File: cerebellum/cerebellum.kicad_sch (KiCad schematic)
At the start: 184 parts, among them J1 PWR_OUT, J2 PWR_IN, J5 CM4_A, J6 CM4_B, J7 RJ45, Q1 AP2300, U1 GD32F405VGHx, U2 TPS5430DDAR, U3 BMI088, U4 TCAN4550RGYRQ1, U5 ICP-20100, U6 TPS54231, U7 TCAN4550RGYRQ1, Y1 8M, Y2 40M, Y3 40M

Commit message: [New] Complete cerebellum
* Refactor cerebellum, now cerebellum includes features of heart &
  cerebellum

Signed-off-by: Homalozoa <nx.tardis@gmail.com>
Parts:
- removed C33, C34: 8.2pF, 10%, 50V, Capacitor_SMD:C_0402_1005Metric, symbol Device:C
- removed C35: 10nF, 10%, 50V, Capacitor_SMD:C_0402_1005Metric, symbol Device:C
- removed C36: 470nF, 10%, 50V, Capacitor_SMD:C_0603_1608Metric, symbol Device:C
- removed C37, C38: 100pF, 10%, 10V, Capacitor_SMD:C_0402_1005Metric, symbol Device:C
- removed C39: 100nF, 10%, 50V, Capacitor_SMD:C_0402_1005Metric, symbol Device:C
- removed C40, C41: 10uF, 10%, 50V, Capacitor_SMD:C_0603_1608Metric, symbol Device:C
- removed C42, C43: 4.7uF 50V, Capacitor_SMD:C_0805_2012Metric, symbol Device:C
- removed C44: 10uf 50V, Capacitor_SMD:C_0402_1005Metric, symbol Device:C
- removed C45: 1.5nf 50V, Capacitor_SMD:C_0603_1608Metric, symbol Device:C
- removed C46: 8.2nf 50V, Capacitor_SMD:C_0603_1608Metric, symbol Device:C
- removed C47: 10pf 50V, Capacitor_SMD:C_0402_1005Metric, symbol Device:C
- removed C48, C? (x11): 100nF, 10%, 10V, Capacitor_SMD:C_0402_1005Metric, symbol Device:C
- removed C49, C50, C? (x12): 47uf 50V, Capacitor_SMD:C_0603_1608Metric, symbol Device:C
- removed C? (x2): 22pF, 10%, 50V, Capacitor_SMD:C_0402_1005Metric, symbol Device:C
- removed C? (x10): 100nF, 10%, 10V, Capacitor_SMD:C_0201_0603Metric, symbol Device:C
- removed C? (x3): 1uF, 10%, 10V, Capacitor_SMD:C_0402_1005Metric, symbol Device:C
- removed C?: 3nF, 10V, Capacitor_SMD:C_0402_1005Metric, symbol Device:C
- removed C? (x2): 10uF, 10%, 10V, Capacitor_SMD:C_0402_1005Metric, symbol Device:C
- removed C?: 4.7uF, 10%, 10V, Capacitor_SMD:C_0402_1005Metric, symbol Device:C
- removed D5: B240, Diode_SMD:D_SMB, symbol Diode:B240
- removed J1: PWR_OUT, Rolling_Custom:XT30PW(2+2), symbol Rolling_Custom:XT30PW(2+2)
- removed J2: PWR_IN, Rolling_Custom:XT30PW(2+2), symbol Rolling_Custom:XT30PW(2+2)
- removed J5: CM4_A, Rolling_Custom:HRS_DF40C-100DS-0.4V(51), symbol Rolling_Custom:DF40C-100DS-0.4V(51)
- removed J6: CM4_B, Rolling_Custom:HRS_DF40C-100DS-0.4V(51), symbol Rolling_Custom:DF40C-100DS-0.4V(51)
- removed J7: RJ45, Connector_RJ:RJ45_Molex_0855135013_Vertical, symbol Connector:RJ45
- removed J? (x4): USB_C_Receptacle, Rolling_Custom:USB_C_Receptacle_TYPE-C-324G-BCP24, symbol Connector:USB_C_Receptacle
- removed J?: (no value), symbol Connector:USB_C_Receptacle_USB2.0
- removed L3: 15uh, Inductor_SMD:L_0603_1608Metric, symbol Device:L
- removed L?: 0R, Resistor_SMD:R_0402_1005Metric, symbol Device:L_Ferrite
- removed R16: 3k, Resistor_SMD:R_0402_1005Metric, symbol Device:R_US
- removed R17: 169k, Resistor_SMD:R_0402_1005Metric, symbol Device:R_US
- removed R18: 20.5, Resistor_SMD:R_0402_1005Metric, symbol Device:R_US
- removed R19: 64.9k, Resistor_SMD:R_0402_1005Metric, symbol Device:R_US
- removed R20: 10.2k, Resistor_SMD:R_0402_1005Metric, symbol Device:R_US
- removed R21: 1.96k, Resistor_SMD:R_0402_1005Metric, symbol Device:R_US
- removed R? (x3): 4.7k, Resistor_SMD:R_0402_1005Metric, symbol Device:R_US
- removed R? (x2): 47k, Resistor_SMD:R_0402_1005Metric, symbol Device:R_US
- removed R?: 2.2k, Resistor_SMD:R_0201_0603Metric, symbol Device:R_US
- removed R?: (no value), Resistor_SMD:R_0201_0603Metric, symbol Device:R_US
- removed R? (x4): 100k, Resistor_SMD:R_0402_1005Metric, symbol Device:R_US
- removed R?: 15k, Resistor_SMD:R_0402_1005Metric, symbol Device:R_US
- removed R?: 1M, Resistor_SMD:R_0402_1005Metric, symbol Device:R_US
- removed U6: TPS54231, Package_SO:SOIC-8_3.9x4.9mm_P1.27mm, symbol Regulator_Switching:TPS54233
- removed U7: TCAN4550RGYRQ1, Rolling_Custom:VQFN20, symbol Rolling_Custom:TCAN4550RGYRQ1
- removed U? (x4): APL3553, Package_TO_SOT_SMD:SOT-23-5, symbol Rolling_Custom:APL3553
- removed U? (x7): TPD4EUSB30, Package_SON:USON-10_2.5x1.0mm_P0.5mm, symbol Power_Protection:TPD4EUSB30
- removed U? (x4): ECMF04-4HSM10, Rolling_Custom:SON_4-4HSM10_STM, symbol Rolling_Custom:ECMF04-4HSM10
- removed U?: AP2127K-ADJ, Package_TO_SOT_SMD:SOT-23-5, symbol Regulator_Linear:AP2127K-ADJ
- removed U? (x4): ECMF02-4CMX8, Rolling_Custom:MICRO_QFN-8L_STM, symbol Rolling_Custom:ECMF02-4CMX8
- removed U?: UPD720201K8-701-BAC-A, Rolling_Custom:QFN40P800X800X90-69N, symbol Rolling_Custom:UPD720201K8-701-BAC-A
- removed U?: GD25Q40C, symbol Rolling_Custom:GD25Q40C
- removed U?: (no value), symbol Power_Protection:TPD4EUSB30
- removed Y3: 40M, Oscillator:Oscillator_SMD_EuroQuartz_XO32-4Pin_3.2x2.5mm, symbol Device:Crystal_GND24
- removed Y?: 24M, Oscillator:Oscillator_SMD_EuroQuartz_XO32-4Pin_3.2x2.5mm, symbol Device:Crystal_GND24
- added FB1: 220R, Resistor_SMD:R_0603_1608Metric, symbol Device:FerriteBead
- added J1: Power_IN, Rolling_Custom:AMASS_XT60PW-F, symbol Rolling_Custom:XT60PW-F
- added J10: Arm_R, Rolling_Custom:XT30PW(2+2), symbol Rolling_Custom:XT30PW(2+2)
- added J11: Light, Rolling_Custom:XT30PW(2+2), symbol Rolling_Custom:XT30PW(2+2)
- added J2: Power_Back, Rolling_Custom:AMASS_XT60PW-M, symbol Rolling_Custom:XT60PW-M
- added J5: Head, Rolling_Custom:XT30PW(2+2), symbol Rolling_Custom:XT30PW(2+2)
- added J7: Leg_L, Rolling_Custom:XT30PW(2+2), symbol Rolling_Custom:XT30PW(2+2)
- added J8: Leg_R, Rolling_Custom:XT30PW(2+2), symbol Rolling_Custom:XT30PW(2+2)
- added J9: Arm_L, Rolling_Custom:XT30PW(2+2), symbol Rolling_Custom:XT30PW(2+2)
- added Q2, Q3, Q4: FH1404G6, Rolling_Custom:PDFN5X6-8L, symbol Rolling_Custom:WNM6006
- J3, J4: value (none) -> GD_LINK
- R8: value 33k -> 120R
- U1: value GD32F405VGHx -> (none); footprint Package_BGA:UFBGA-100_7x7mm_Layout12x12_P0.5mm -> Rolling_Custom:Modified-BGA-100_7x7mm_Layout12x12_P0.5mm
- gave numbers to parts that had none: 1
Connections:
- net TCANPi_WAKE is gone; now on net CAN_H: R8.1
- net +24V: now also J1.1 (+), Q2.5
- net ACC_SCS: now also U1.A12 (PA12); no longer U1.A9 (PA15)
- net BMI_HEAT: now also U1.A3 (PB8); no longer U1.H10 (PD15)
- net CAN_H: now also J10.3 (CAN_H), J11.3 (CAN_H), J5.3 (CAN_H), J7.3 (CAN_H), J8.3 (CAN_H), J9.3 (CAN_H)
- net CAN_L: now also R8.2, J10.4 (CAN_L), J11.4 (CAN_L), J5.4 (CAN_L), J7.4 (CAN_L), J8.4 (CAN_L), J9.4 (CAN_L)
- net GND: now also FB1.2; no longer C13.2, D1.1 (A1)
- net GYRO_SCS: now also U1.A9 (PA15); no longer U1.A12 (PA12)
- net PWRCT_3: now reaches U1.A1 (PE3)
- net PWRCT_3: now also Q4.4
- net PWRCT_2: now reaches U1.B1 (PE4)
- net PWRCT_2: now also Q3.4
- net PWRCT_1: now reaches U1.C1 (PC13)
- net PWRCT_1: now also Q2.4
- net BMI_INT1: no longer names the net of U3.16 (INT1)
- net BMI_INT1: no longer U1.E10 (PC8)
- net BMI_INT2: no longer names the net of U3.1 (INT2)
- net BMI_INT2: no longer U1.D10 (PA9)
- net BMI_INT3: no longer names the net of U3.12 (INT3)
- net BMI_INT3: no longer U1.C8 (PD2)
- net BMI_INT4: no longer names the net of U3.13 (INT4)
- net BMI_INT4: no longer U1.B7 (PD4)
- new net EXT_PWR: J2.1 (+), Q3.5, Q4.1, Q4.2, Q4.3
- new net GNDA: C13.2, D1.1 (A1), FB1.1, J1.2 (-), J1.S1 (SHIELD), J1.S2 (SHIELD), J10.2 (GND), J11.2 (GND), J2.2 (-), J2.S1 (SHIELD), J2.S2 (SHIELD), J5.2 (GND), J7.2 (GND), J8.2 (GND), J9.2 (GND)
- new net PWR_EXPORT: J10.1 (VBUS), J11.1 (VBUS), J5.1 (VBUS), J7.1 (VBUS), J8.1 (VBUS), J9.1 (VBUS), Q2.1, Q2.2, Q2.3, Q3.1, Q3.2, Q3.3, Q4.5
- no-connect marks 169 -> 65
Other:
- moved on the sheet: C1, C10, C11, C12, C13, C14, C15, C16, C17, C18, C19, C2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

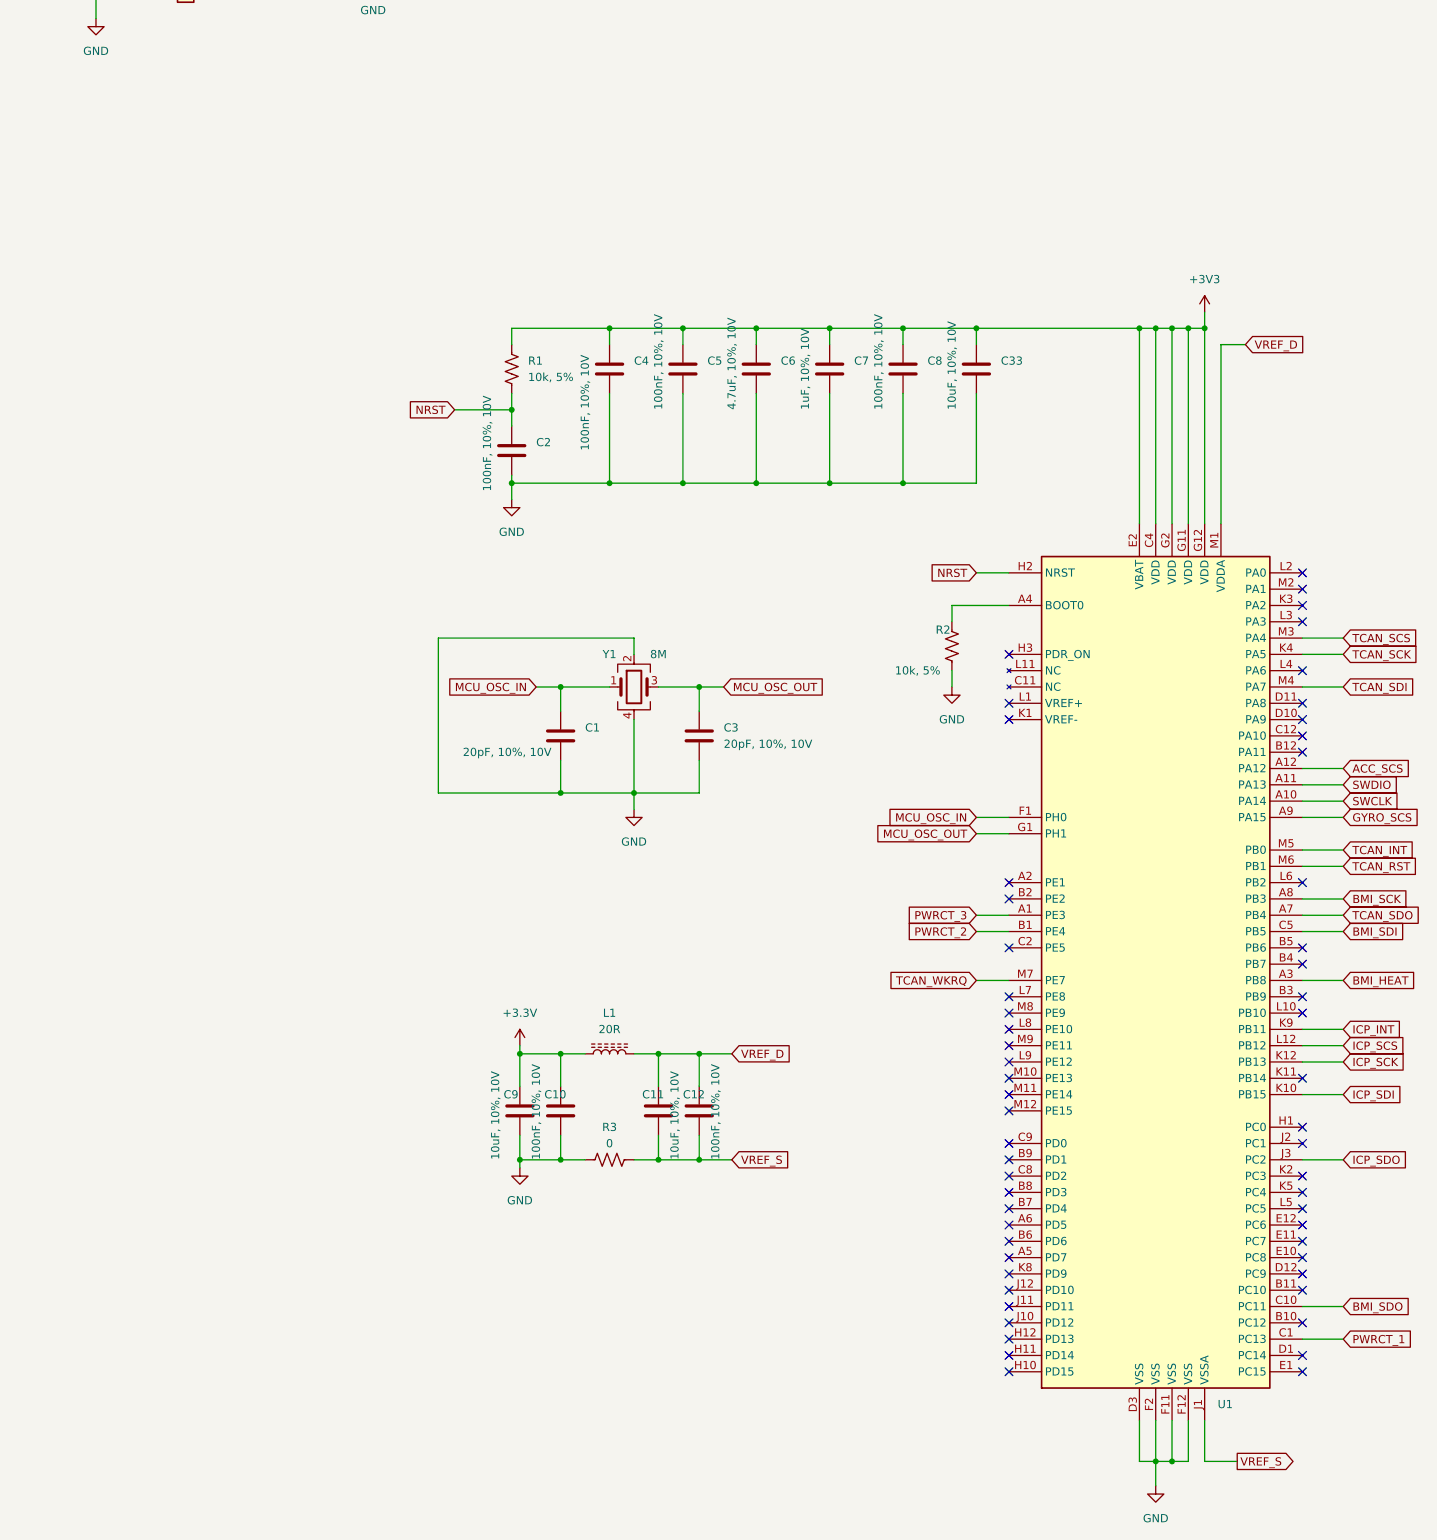
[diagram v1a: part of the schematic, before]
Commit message: [New] Add some capacities to cerebellum
Signed-off-by: Homalozoa <nx.tardis@gmail.com>
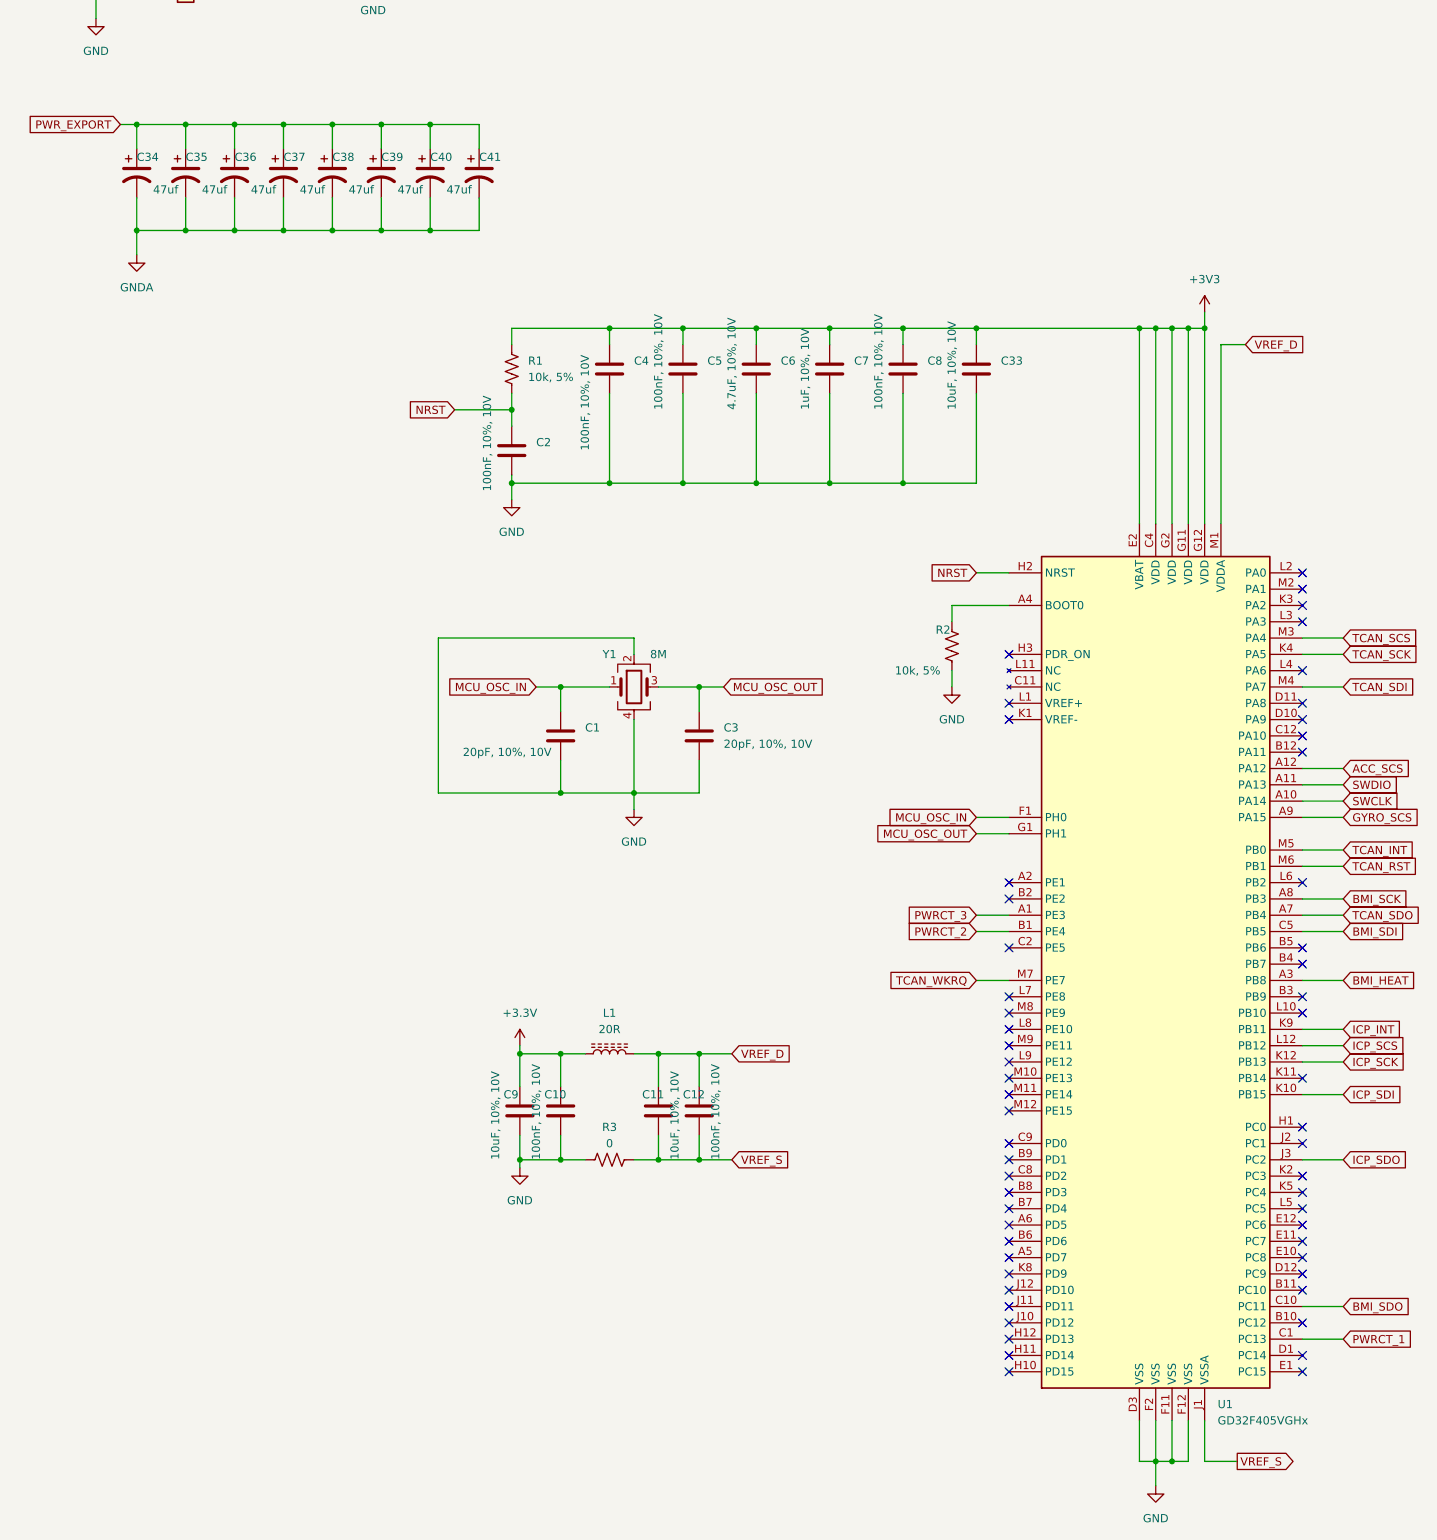
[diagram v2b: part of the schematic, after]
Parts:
- added C34: (no value), symbol Device:C_Polarized_US
- added C35, C36, C37, C38, C39, C40, C41: 47uf, Capacitor_SMD:CP_Elec_8x6.2, symbol Device:C_Polarized_US
- U1: value (none) -> GD32F405VGHx
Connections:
- net GNDA: now also C34.2, C35.2, C36.2, C37.2, C38.2, C39.2, C40.2, C41.2
- net PWR_EXPORT: now also C34.1, C35.1, C36.1, C37.1, C38.1, C39.1, C40.1, C41.1

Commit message: [Fix] Fix package of diode in cerebellum
Signed-off-by: Homalozoa <nx.tardis@gmail.com>
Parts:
- C34: value (none) -> 47uf; footprint (none) -> Capacitor_SMD:CP_Elec_8x6.2
- D1: value 30V -> (none); footprint Diode_SMD:D_SMA -> (none)
- D2: value B340 -> ESD5Z3V3; footprint Diode_SMD:D_SMC -> Diode_SMD:D_SOD-523
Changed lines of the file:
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@@
       (effects (font (size 1.27 1.27)) (justify right))
     )
-    (property "Value" "30V" (id 1) (at 353.06 100.33 90)
-      (effects (font (size 1.27 1.27)) (justify right))
-    )
-    (property "Footprint" "Diode_SMD:D_SMA" (id 2) (at 360.68 99.06 0)
+    (property "Value" "" (id 1) (at 353.06 100.33 90)
+      (effects (font (size 1.27 1.27)) (justify right))
+    )
+    (property "Footprint" "" (id 2) (at 360.68 99.06 0)
       (effects (font (size 1.27 1.27)) hide)
     )
@@
       (effects (font (size 1.27 1.27)) (justify left))
     )
-    (property "Value" "" (id 1) (at 44.45 166.37 0)
-      (effects (font (size 1.27 1.27)) (justify left))
-    )
-    (property "Footprint" "" (id 2) (at 49.53 163.83 0)
+    (property "Value" "47uf" (id 1) (at 44.45 166.37 0)
+      (effects (font (size 1.27 1.27)) (justify left))
+    )
+    (property "Footprint" "Capacitor_SMD:CP_Elec_8x6.2" (id 2) (at 49.53 163.83 0)
       (effects (font (size 1.27 1.27)) hide)
     )
@@
     (pin "1")
   )
+  (symbol (lib_id "Diode:B340") (at 445.77 104.14 270) (unit 1)
+    (in_bom yes) (on_board yes) (fields_autoplaced)
+    (property "Reference" "D2" (id 0) (at 448.31 102.5524 90)
+      (effects (font (size 1.27 1.27)) (justify left))
+    )
+    (property "Value" "ESD5Z3V3" (id 1) (at 448.31 105.0924 90)
+      (effects (font (size 1.27 1.27)) (justify left))
+    )
+    (property "Footprint" "Diode_SMD:D_SOD-523" (id 2) (at 441.325 104.14 0)
+      (effects (font (size 1.27 1.27)) hide)
+    )
+    (property "Datasheet" "http://www.jameco.com/Jameco/Products/ProdDS/1538777.pdf" (id 3) (at 445.77 104.14 0)
+      (effects (font (size 1.27 1.27)) hide)
+    )
+    (pin "1")
+    (pin "2")
+  )
   (symbol (lib_id "Device:C_Polarized_US") (at 80.01 163.83 0) (unit 1)
     (in_bom yes) (on_board yes)
@@
     (pin "2")
   )
-  (symbol (lib_id "Diode:B340") (at 445.77 104.14 270) (unit 1)
-    (in_bom yes) (on_board yes) (fields_autoplaced)
-    (property "Reference" "D2" (id 0) (at 448.31 102.5524 90)
-      (effects (font (size 1.27 1.27)) (justify left))
-    )
-    (property "Value" "B340" (id 1) (at 448.31 105.0924 90)
-      (effects (font (size 1.27 1.27)) (justify left))
-    )
-    (property "Footprint" "Diode_SMD:D_SMC" (id 2) (at 441.325 104.14 0)
-      (effects (font (size 1.27 1.27)) hide)
-    )
-    (property "Datasheet" "http://www.jameco.com/Jameco/Products/ProdDS/1538777.pdf" (id 3) (at 445.77 104.14 0)
-      (effects (font (size 1.27 1.27)) hide)
-    )
-    (pin "1")
-    (pin "2")
-  )
   (symbol (lib_id "Device:C") (at 180.34 194.31 0) (unit 1)
     (in_bom yes) (on_board yes)
@@
     )
     (path "/8875e8b5-e0bd-4a1d-a368-3553513f8fa7"
-      (reference "D1") (unit 1) (value "30V") (footprint "Diode_SMD:D_SMA")
-    )
-    (path "/fd3a09ae-9752-49b5-a1c6-af75b4c89eb0"
-      (reference "D2") (unit 1) (value "B340") (footprint "Diode_SMD:D_SMC")
+      (reference "D1") (unit 1) (value "SMF30CA") (footprint "Diode_SMD:D_SOD-123")
+    )
+    (path "/f34be9c3-64e1-4326-a6cf-b85cf1241afa"
+      (reference "D2") (unit 1) (value "ESD5Z3V3") (footprint "Diode_SMD:D_SOD-523")
     )
     (path "/d6cf48a9-a13f-466f-bfde-8bc93913d1c0"

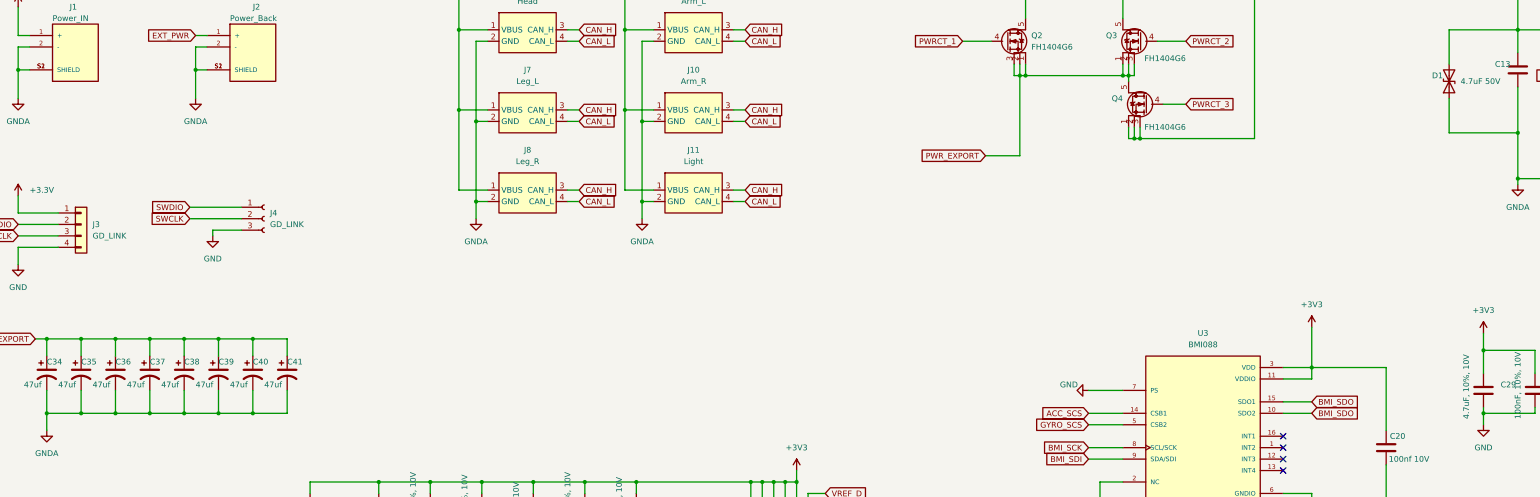
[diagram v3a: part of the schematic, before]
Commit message: [New] Refactoring placement & routing of cerebellum
Signed-off-by: Homalozoa <nx.tardis@gmail.com>
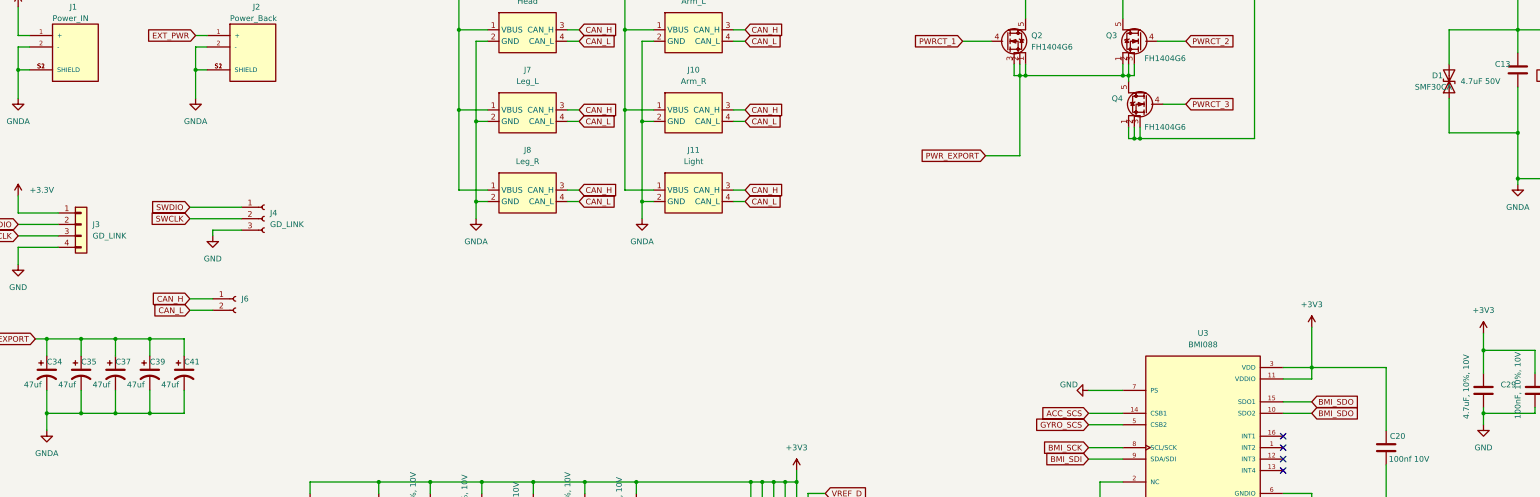
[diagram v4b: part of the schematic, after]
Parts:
- removed C36, C38, C40: 47uf, Capacitor_SMD:CP_Elec_8x6.2, symbol Device:C_Polarized_US
- added J6: (no value), symbol Connector:Conn_01x02_Female
- D1: value (none) -> SMF30CA; footprint (none) -> Diode_SMD:D_SOD-123
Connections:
- net CAN_H: now also J6.1 (Pin_1)
- net CAN_L: now also J6.2 (Pin_2)
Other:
- moved on the sheet: C37, C39, C41
